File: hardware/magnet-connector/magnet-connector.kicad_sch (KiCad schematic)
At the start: 1 part, among them U1 WS2812-2020

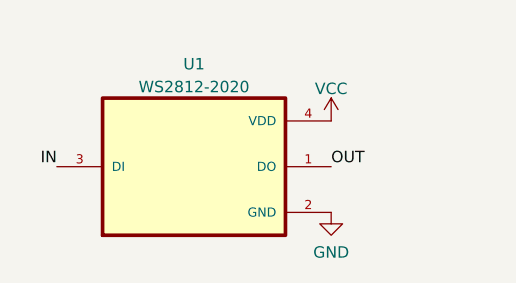
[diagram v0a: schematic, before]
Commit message: Update magnet connector with correct dimensions
Change-Id: I8f117cb6aa70f2da7e4e38435df749311b8c2ee4
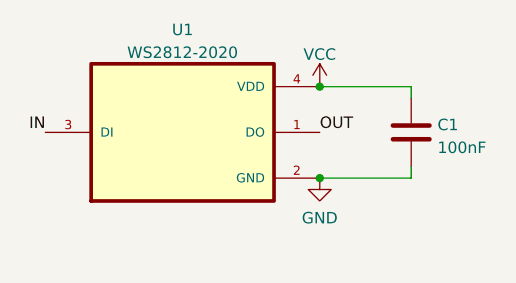
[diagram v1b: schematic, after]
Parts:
- added C1: 100nF, Capacitor_SMD:C_0402_1005Metric, symbol Device:C
- U1: footprint Homebrew:LED_WS2812-2020 -> LED_WS2812-2020; STANDARD (none) -> Manufacturer Recommendations
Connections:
- net GND: now also C1.2
- net VCC: now also C1.1
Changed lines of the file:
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@@
 (kicad_sch (version 20211123) (generator eeschema)
   (paper "A4")
-  (label "IN" (at 97.79 38.1 180)
+  (junction (at 127 29.21) (diameter 0) (color 0 0 0 0)
+  )
+  (junction (at 127 39.37) (diameter 0) (color 0 0 0 0)
+  )
+  (wire (pts (xy 127 39.37) (xy 137.16 39.37))
+    (stroke (width 0) (type default) (color 0 0 0 0))
+  )
+  (wire (pts (xy 127 29.21) (xy 137.16 29.21))
+    (stroke (width 0) (type default) (color 0 0 0 0))
+  )
+  (wire (pts (xy 137.16 39.37) (xy 137.16 38.1))
+    (stroke (width 0) (type default) (color 0 0 0 0))
+  )
+  (wire (pts (xy 137.16 30.48) (xy 137.16 29.21))
+    (stroke (width 0) (type default) (color 0 0 0 0))
+  )
+  (label "IN" (at 96.52 34.29 180)
     (effects (font (size 1.27 1.27)) (justify right bottom))
   )
-  (label "OUT" (at 128.27 38.1 0)
+  (label "OUT" (at 127 34.29 0)
     (effects (font (size 1.27 1.27)) (justify left bottom))
   )
-  (symbol (lib_id "power:GND") (at 128.27 43.18 0) (unit 1)
+  (symbol (lib_id "Device:C") (at 137.16 34.29 0) (unit 1)
     (in_bom yes) (on_board yes) (fields_autoplaced)
-    (property "Reference" "#PWR0101" (id 0) (at 128.27 49.53 0)
+    (property "Reference" "C1" (id 0) (at 140.081 33.4553 0)
+      (effects (font (size 1.27 1.27)) (justify left))
+    )
+    (property "Value" "100nF" (id 1) (at 140.081 35.9922 0)
+      (effects (font (size 1.27 1.27)) (justify left))
+    )
+    (property "Footprint" "Capacitor_SMD:C_0402_1005Metric" (id 2) (at 138.1252 38.1 0)
       (effects (font (size 1.27 1.27)) hide)
     )
-    (property "Value" "GND" (id 1) (at 128.27 47.6234 0))
-    (property "Footprint" "" (id 2) (at 128.27 43.18 0)
+    (property "Datasheet" "~" (id 3) (at 137.16 34.29 0)
       (effects (font (size 1.27 1.27)) hide)
     )
-    (property "Datasheet" "" (id 3) (at 128.27 43.18 0)
+    (pin "1")
+    (pin "2")
+  )
+  (symbol (lib_id "power:GND") (at 127 39.37 0) (unit 1)
+    (in_bom yes) (on_board yes) (fields_autoplaced)
+    (property "Reference" "#PWR0101" (id 0) (at 127 45.72 0)
+      (effects (font (size 1.27 1.27)) hide)
+    )
+    (property "Value" "GND" (id 1) (at 127 43.8134 0))
+    (property "Footprint" "" (id 2) (at 127 39.37 0)
+      (effects (font (size 1.27 1.27)) hide)
+    )
+    (property "Datasheet" "" (id 3) (at 127 39.37 0)
       (effects (font (size 1.27 1.27)) hide)
     )
     (pin "1")
   )
-  (symbol (lib_id "power:VCC") (at 128.27 33.02 0) (unit 1)
+  (symbol (lib_id "Homebrew:WS2812-2020") (at 111.76 34.29 0) (unit 1)
     (in_bom yes) (on_board yes) (fields_autoplaced)
-    (property "Reference" "#PWR0102" (id 0) (at 128.27 36.83 0)
-      (effects (font (size 1.27 1.27)) hide)
-    )
-    (property "Value" "VCC" (id 1) (at 128.27 29.4442 0))
-    (property "Footprint" "" (id 2) (at 128.27 33.02 0)
-      (effects (font (size 1.27 1.27)) hide)
-    )
-    (property "Datasheet" "" (id 3) (at 128.27 33.02 0)
-      (effects (font (size 1.27 1.27)) hide)
-    )
-    (pin "1")
-  )
-  (symbol (lib_id "Homebrew:WS2812-2020") (at 113.03 38.1 0) (unit 1)
-    (in_bom yes) (on_board yes) (fields_autoplaced)
-    (property "Reference" "U1" (id 0) (at 113.03 26.704 0))
-    (property "Value" "WS2812-2020" (id 1) (at 113.03 29.2409 0))
-    (property "Footprint" "Homebrew:LED_WS2812-2020" (id 2) (at 113.03 38.1 0)
+    (property "Reference" "U1" (id 0) (at 111.76 22.894 0))
+    (property "Value" "WS2812-2020" (id 1) (at 111.76 25.4309 0))
+    (property "Footprint" "LED_WS2812-2020" (id 2) (at 111.76 34.29 0)
       (effects (font (size 1.27 1.27)) (justify left bottom) hide)
     )
-    (property "Datasheet" "" (id 3) (at 113.03 38.1 0)
+    (property "Datasheet" "" (id 3) (at 111.76 34.29 0)
       (effects (font (size 1.27 1.27)) (justify left bottom) hide)
     )
-    (property "MANUFACTURER" "Worldsemi" (id 5) (at 113.03 38.1 0)
+    (property "STANDARD" "Manufacturer Recommendations" (id 4) (at 111.76 34.29 0)
+      (effects (font (size 1.27 1.27)) (justify left bottom) hide)
+    )
+    (property "MANUFACTURER" "Worldsemi" (id 5) (at 111.76 34.29 0)
       (effects (font (size 1.27 1.27)) (justify left bottom) hide)
     )
@@
     (pin "3")
     (pin "4")
+  )
+  (symbol (lib_id "power:VCC") (at 127 29.21 0) (unit 1)
+    (in_bom yes) (on_board yes)
+    (property "Reference" "#PWR0104" (id 0) (at 127 33.02 0)
+      (effects (font (size 1.27 1.27)) hide)
+    )
+    (property "Value" "VCC" (id 1) (at 127 25.6342 0))
+    (property "Footprint" "" (id 2) (at 127 29.21 0)
+      (effects (font (size 1.27 1.27)) hide)
+    )
+    (property "Datasheet" "" (id 3) (at 127 29.21 0)
+      (effects (font (size 1.27 1.27)) hide)
+    )
+    (pin "1")
   )
   (sheet_instances
@@
       (reference "#PWR0101") (unit 1) (value "GND") (footprint "")
     )
-    (path "/b924b507-e45f-4671-b21c-41bb91ec9dfe"
-      (reference "#PWR0102") (unit 1) (value "VCC") (footprint "")
+    (path "/ce1b8f4f-995c-494a-822e-b8be9f689fd9"
+      (reference "#PWR0104") (unit 1) (value "VCC") (footprint "")
     )
-    (path "/cee6d385-179f-441e-ba5b-f09f427543bc"
-      (reference "U1") (unit 1) (value "WS2812-2020") (footprint "Homebrew:LED_WS2812-2020")
+    (path "/04d55d1c-012c-4c8b-a372-b53f95cea924"
+      (reference "C1") (unit 1) (value "100nF") (footprint "Capacitor_SMD:C_0402_1005Metric")
+    )
+    (path "/7deca6cd-fff6-4137-8732-d86b2257c8d4"
+      (reference "U1") (unit 1) (value "WS2812-2020") (footprint "LED_WS2812-2020")
     )
   )
